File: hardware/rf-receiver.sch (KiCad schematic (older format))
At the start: 33 parts, among them IC1 ATSAMD21G18A-AU, J3 USB_C_Receptacle, P1 ROT_ENC, SW1 BTN1, SW2 BTN2, SW3 BTN3, U1 74HC14, Y1 Crystal_Small

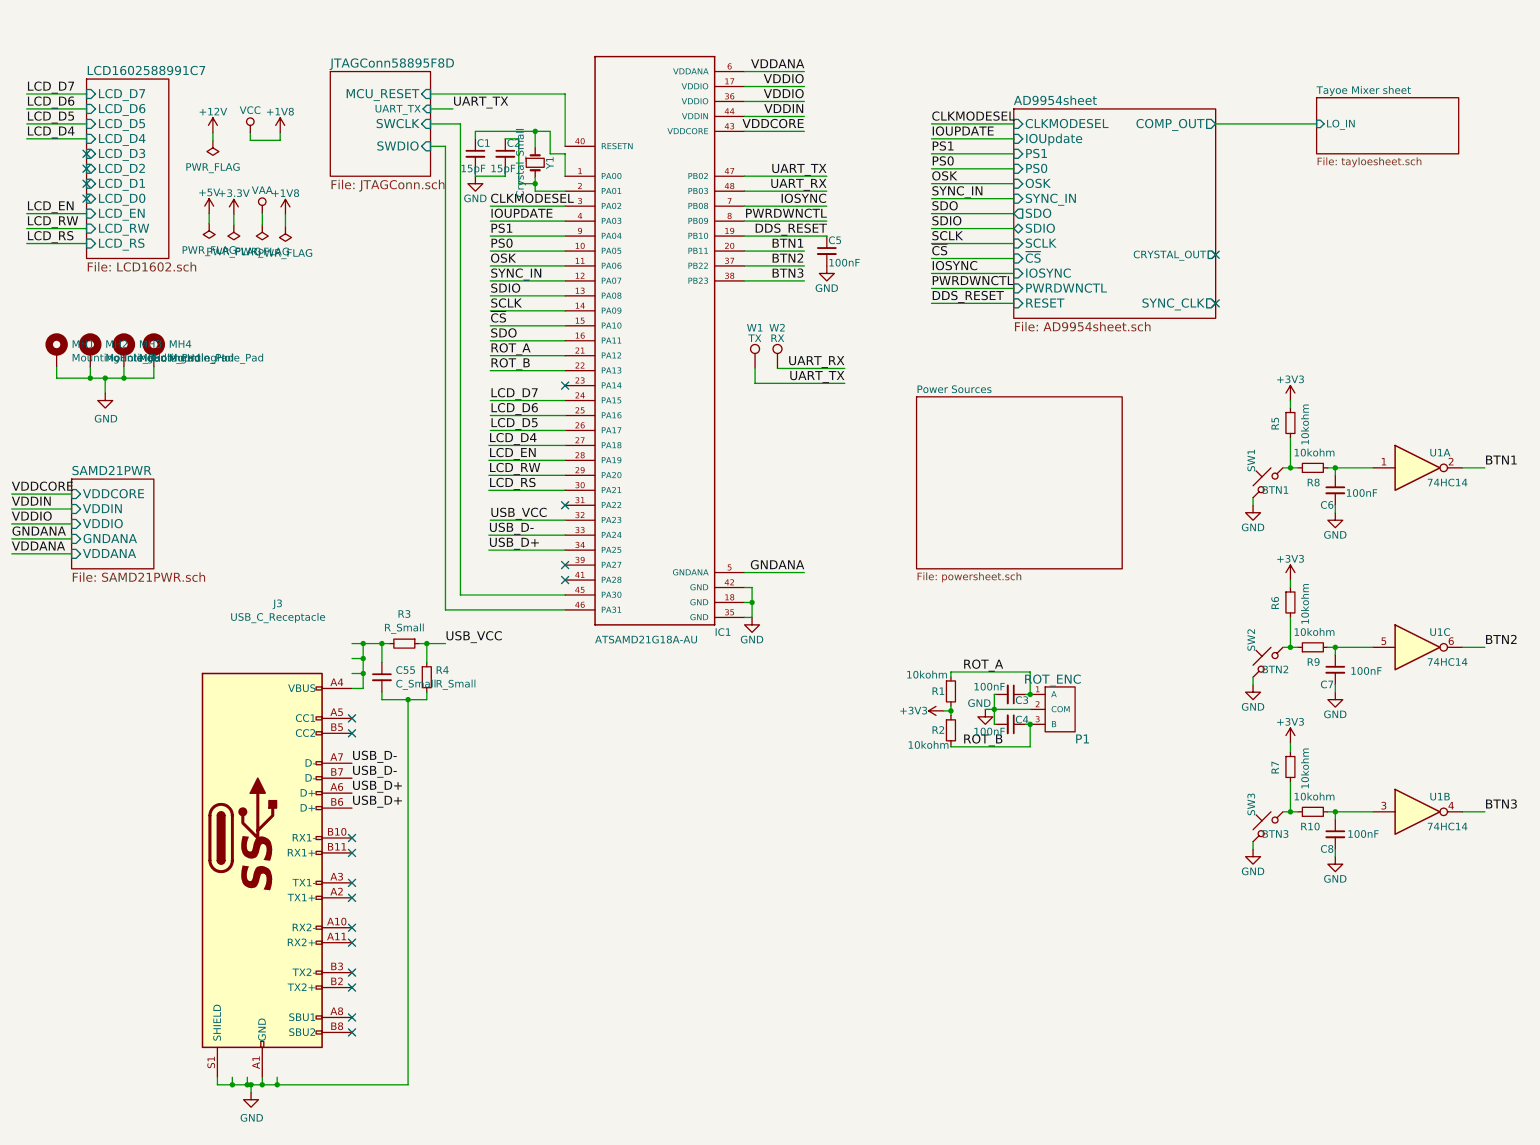
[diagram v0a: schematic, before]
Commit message: Finished work on Receiver RPi shield. Changed CLK to SI5351A. Minimized footprints for almost all Tayloe detector ICs. Added -12V to audio opamps. Prepared board for coexisting with Hifiberry.
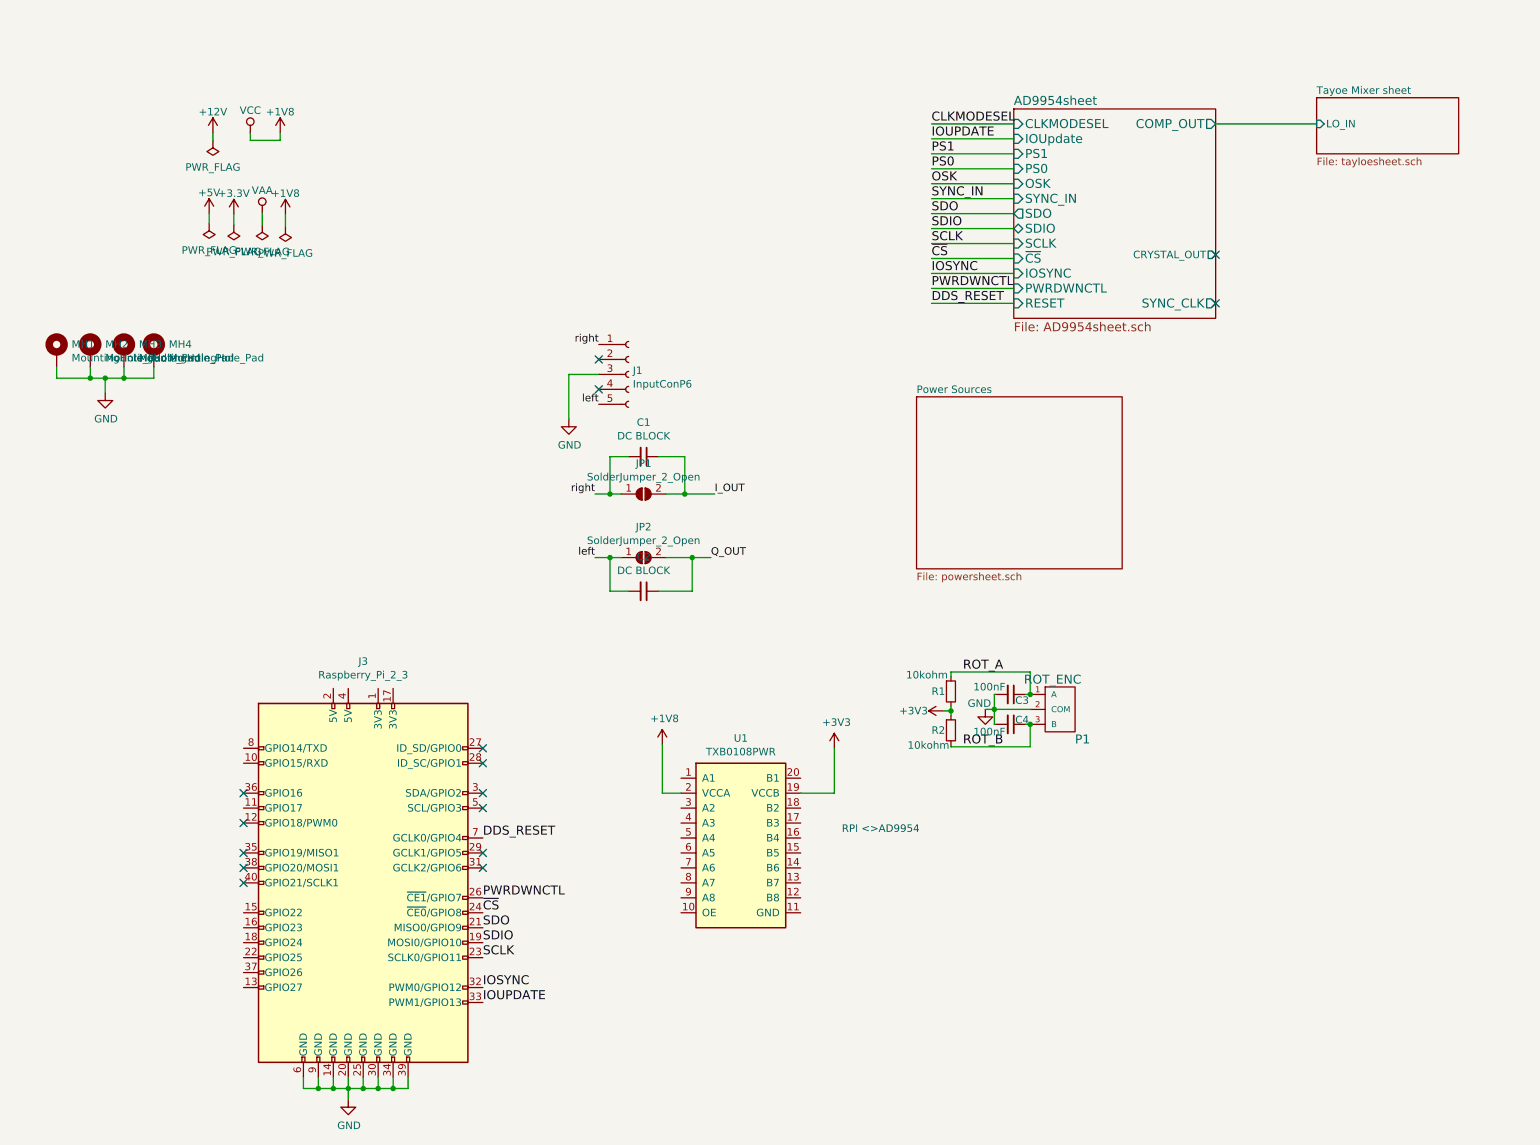
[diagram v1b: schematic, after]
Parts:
- removed C5, C6, C7, C8: 100nF, Capacitor_SMD:C_0603_1608Metric, symbol Device:C_Small
- removed C55: C_Small, Capacitor_SMD:C_0603_1608Metric, symbol Device:C_Small
- removed IC1: ATSAMD21G18A-AU, Package_QFP:TQFP-48_7x7mm_P0.5mm, symbol athir:ATSAMD21G18A-AU
- removed J3: USB_C_Receptacle, athir:DX07S024JJ, symbol Connector:USB_C_Receptacle
- removed R10, R5, R6, R7, R8, R9: 10kohm, Resistor_SMD:R_0603_1608Metric, symbol Device:R_Small
- removed R3, R4: R_Small, Resistor_SMD:R_0603_1608Metric, symbol Device:R_Small
- removed SW1: BTN1, Connector_PinHeader_2.54mm:PinHeader_1x02_P2.54mm_Vertical, symbol Switch:SW_Push_45deg
- removed SW2: BTN2, Connector_PinHeader_2.54mm:PinHeader_1x02_P2.54mm_Vertical, symbol Switch:SW_Push_45deg
- removed SW3: BTN3, Connector_PinHeader_2.54mm:PinHeader_1x02_P2.54mm_Vertical, symbol Switch:SW_Push_45deg
- removed U1: 74HC14, Package_SO:TSSOP-14_4.4x5mm_P0.65mm, symbol 74xx:74HC14
- removed W1: TX, TestPoint:TestPoint_THTPad_2.0x2.0mm_Drill1.0mm, symbol Connector:TestPoint
- removed W2: RX, TestPoint:TestPoint_THTPad_2.0x2.0mm_Drill1.0mm, symbol Connector:TestPoint
- removed Y1: Crystal_Small, Crystal:Crystal_SMD_3215-2Pin_3.2x1.5mm, symbol Device:Crystal_Small
- added J1: InputConP6, Connector_PinHeader_2.54mm:PinHeader_1x05_P2.54mm_Vertical, symbol Connector:Conn_01x05_Female
- added J3: Raspberry_Pi_2_3, Connector_PinHeader_2.54mm:PinHeader_2x20_P2.54mm_Vertical, symbol Connector:Raspberry_Pi_2_3
- added JP1, JP2: SolderJumper_2_Open, symbol Jumper:SolderJumper_2_Open
- added U1: TXB0108PWR, TO_SOT_Packages_SMD:USON-20_2x4mm_Pitch0.4mm, symbol athir:TXB0108PWR
- C1, C2: value 15pF -> DC BLOCK
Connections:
- net labels added: I_OUT, Q_OUT, left, right
- net labels removed: BTN1, BTN2, BTN3, GNDANA, LCD_D4, LCD_D5, LCD_D6, LCD_D7, LCD_EN, LCD_RS, LCD_RW, UART_RX, UART_TX, USB_D+, USB_D-, USB_VCC, VDDANA, VDDCORE, VDDIN, VDDIO
- wire segments 189 -> 86
- no-connect marks 22 -> 15
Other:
- note added: "RPI <>AD9954"

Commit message: Added rpi changes - seems weird that I forgot that for so long
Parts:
- removed JP1, JP2: SolderJumper_2_Open, symbol Jumper:SolderJumper_2_Open
- removed U1: TXB0108PWR, TO_SOT_Packages_SMD:USON-20_2x4mm_Pitch0.4mm, symbol athir:TXB0108PWR
- added C14, C15: 39pF, Capacitor_SMD:C_0603_1608Metric, symbol Device:C_Small
- added C16, C17, C20, C23: 100nF, Capacitor_SMD:C_0603_1608Metric, symbol Device:C_Small
- added C18, C19: 10uF, Capacitor_SMD:C_0603_1608Metric, symbol Device:C_Small
- added C7: 22uF, Capacitor_SMD:C_0805_2012Metric, symbol Device:C_Small
- added D1, D2: LED, Diode_SMD:D_1206_3216Metric, symbol Device:LED
- added J8: RF_Shield_One_Piece, RF_Shielding:Laird_Technologies_BMI-S-101_13.66x12.70mm, symbol Device:RF_Shield_One_Piece
- added JP1: Jumper_2_Open, Connector_PinHeader_2.54mm:PinHeader_1x02_P2.54mm_Vertical, symbol Jumper:Jumper_2_Open
- added R3, R9: 100, Resistor_SMD:R_0805_2012Metric, symbol Device:R_Small
- added R4: 1k, Resistor_SMD:R_0603_1608Metric, symbol Device:R_Small
- added R5, R8: 3k9, Resistor_SMD:R_0603_1608Metric, symbol Device:R_Small
- added R6, R7: I2CPULLUP, Resistor_SMD:R_0603_1608Metric, symbol Device:R_Small
- added TP13: SCL, athir:testpoint_probe, symbol Connector:TestPoint
- added TP2: SDA, athir:testpoint_probe, symbol Connector:TestPoint
- added U1: MIC5504-3.3YM5, Package_TO_SOT_SMD:SOT-23-5, symbol Regulator_Linear:MIC5504-3.3YM5
- added U2: CAT24C128, Package_SO:SOIC-8_3.9x4.9mm_P1.27mm, symbol Memory_EEPROM:CAT24C128
- added U3: SI5351A-B-GT, digikey-footprints:MSOP-10_W3mm, symbol dk_Clock-Timing-Clock-Generators-PLLs-Frequency-Synthesizers:SI5351A-B-GT
- added Y1: 25MHz 20pF, Crystal:Crystal_SMD_3225-4Pin_3.2x2.5mm, symbol Device:Crystal_GND24
- J1: footprint Connector_PinHeader_2.54mm:PinHeader_1x05_P2.54mm_Vertical -> Connector_PinSocket_2.54mm:PinSocket_1x05_P2.54mm_Vertical
- J3: footprint Connector_PinHeader_2.54mm:PinHeader_2x20_P2.54mm_Vertical -> Connector_PinSocket_2.54mm:PinSocket_2x20_P2.54mm_Vertical
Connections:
- net +3V3: now also C23.2, R4.1, R5.1, R8.1, U2.8 (VCC)
- net +5V: now also J3.2 (5V), J3.4 (5V), C18.1, C7.1, U1.1 (VIN), U1.3 (EN)
- net GND: now also C14.1, C15.1, C16.2, C17.1, C18.2, C19.2, C20.2, C23.1, C7.2, D1.1 (K), D2.1 (K), J8.1 (Shield), JP1.2 (B), U1.2 (GND), U2.1 (A0), U2.2 (A1), U2.3 (A2), U2.4 (GND), U3.8 (GND), Y1.2, Y1.4
- net ROT_A: now also J3.15 (GPIO22)
- net ROT_B: now also J3.16 (GPIO23)
- net SDA: now reaches J3.3 (SDA/GPIO2)
- net SDA: now also R7.2, R8.2, TP2.1, U2.5 (SDA), U3.5 (SDA)
- net SCL: now reaches J3.5 (SCL/GPIO3)
- net SCL: now also R5.2, R6.2, TP13.1, U2.6 (SCL), U3.4 (SCL)
- net DDS_RESET: no longer names the net of J3.7 (GCLK0/GPIO4)
- net IOSYNC: no longer names the net of J3.32 (PWM0/GPIO12)
- net IOSYNC: now also R3.1
- net IOUPDATE: no longer names the net of J3.33 (PWM1/GPIO13)
- net IOUPDATE: now also R9.1
- net PWRDWNCTL: no longer names the net of J3.26 (~CE1~/GPIO7)
- net SCLK: no longer names the net of J3.23 (SCLK0/GPIO11)
- net SDIO: no longer names the net of J3.19 (MOSI0/GPIO10)
- net SDO: no longer names the net of J3.21 (MISO0/GPIO9)
- net ~CS: no longer names the net of J3.24 (~CE0~/GPIO8)
- new net: C15.2, U3.2 (XA), Y1.1
- new net: C14.2, U3.3 (XB), Y1.3
- new net: D1.2 (A), R3.2
- new net: JP1.1 (A), R4.2, U2.7 (WP)
- new net: D2.2 (A), R9.2
- new net +3.3VA: C16.1, C17.2, C19.1, C20.1, R6.1, R7.1, U1.5 (VOUT), U3.1 (VDD), U3.7 (VDDO)
- new net Tayoe Mixer sheet/LO_IN: U3.10 (CLK0)
- no-connect marks 15 -> 28
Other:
- note removed: "RPI <>AD9954"

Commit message: HW: Fixed SMA footprint and 74x3253 footprint
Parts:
- added TP16, TP17: TestPoint, athir:testpoint_probe, symbol Connector:TestPoint
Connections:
- net GND: now also TP17.1
- net Tayoe Mixer sheet/LO_IN: now also TP16.1
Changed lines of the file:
@@
 Connection ~ 10075 5575
 Wire Wire Line
-	8900 1075 9250 1075
+	8900 1075 9150 1075
 Wire Wire Line
 	9250 1075 9250 1100
@@
 Wire Wire Line
 	4835 6710 4835 6830
+$Comp
+L Connector:TestPoint TP16
+U 1 1 5E57B516
+P 9150 975
+F 0 "TP16" H 9208 1093 50  0000 L CNN
+F 1 "TestPoint" H 9208 1002 50  0000 L CNN
+F 2 "athir:testpoint_probe" H 9350 975 50  0001 C CNN
+F 3 "~" H 9350 975 50  0001 C CNN
+	1    9150 975
+	1    0    0    -1
+$EndComp
+Wire Wire Line
+	9150 975  9150 1075
+Connection ~ 9150 1075
+Wire Wire Line
+	9150 1075 9250 1075
+$Comp
+L Connector:TestPoint TP17
+U 1 1 5E58AEC5
+P 9150 1375
+F 0 "TP17" H 9208 1493 50  0000 L CNN
+F 1 "TestPoint" H 9208 1402 50  0000 L CNN
+F 2 "athir:testpoint_probe" H 9350 1375 50  0001 C CNN
+F 3 "~" H 9350 1375 50  0001 C CNN
+	1    9150 1375
+	1    0    0    -1
+$EndComp
+$Comp
+L power:GND #PWR03
+U 1 1 5E58B9E2
+P 9150 1450
+F 0 "#PWR03" H 9150 1200 50  0001 C CNN
+F 1 "GND" H 9155 1277 50  0000 C CNN
+F 2 "" H 9150 1450 50  0001 C CNN
+F 3 "" H 9150 1450 50  0001 C CNN
+	1    9150 1450
+	1    0    0    -1
+$EndComp
+Wire Wire Line
+	9150 1450 9150 1375
 $EndSCHEMATC

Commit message: Sorry future me
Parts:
- added C31: 22uF, Capacitor_SMD:C_0805_2012Metric, symbol Device:C_Small
- added C32: 100nF, Capacitor_SMD:C_0603_1608Metric, symbol Device:C_Small
- added TP20, TP21: TestPoint, athir:testpoint_probe, symbol Connector:TestPoint
- MH1, MH2, MH3, MH4: footprint MountingHole:MountingHole_2.7mm_M2.5_Pad -> MountingHole:MountingHole_3.2mm_M3_Pad
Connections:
- net +5V: now also C31.1, C32.2
- net GND: now also C31.2, C32.1
- net at U3.6 (CLK2): now also TP21.1
- net at U3.9 (CLK1): now also TP20.1
- no-connect marks 28 -> 26
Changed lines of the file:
@@
 $Descr A4 11693 8268
 encoding utf-8
-Sheet 1 3
+Sheet 1 4
 Title ""
 Date "2019-01-20"
@@
 F 0 "MH1" H 1100 2676 50  0000 L CNN
 F 1 "MountingHole_Pad" H 1100 2585 50  0000 L CNN
-F 2 "MountingHole:MountingHole_2.7mm_M2.5_Pad" H 1000 2625 50  0001 C CNN
+F 2 "MountingHole:MountingHole_3.2mm_M3_Pad" H 1000 2625 50  0001 C CNN
 F 3 "~" H 1000 2625 50  0001 C CNN
 	1    1000 2625
@@
 F 0 "MH2" H 1325 2676 50  0000 L CNN
 F 1 "MountingHole_Pad" H 1325 2585 50  0000 L CNN
-F 2 "MountingHole:MountingHole_2.7mm_M2.5_Pad" H 1225 2625 50  0001 C CNN
+F 2 "MountingHole:MountingHole_3.2mm_M3_Pad" H 1225 2625 50  0001 C CNN
 F 3 "~" H 1225 2625 50  0001 C CNN
 	1    1225 2625
@@
 F 0 "MH3" H 1550 2676 50  0000 L CNN
 F 1 "MountingHole_Pad" H 1550 2585 50  0000 L CNN
-F 2 "MountingHole:MountingHole_2.7mm_M2.5_Pad" H 1450 2625 50  0001 C CNN
+F 2 "MountingHole:MountingHole_3.2mm_M3_Pad" H 1450 2625 50  0001 C CNN
 F 3 "~" H 1450 2625 50  0001 C CNN
 	1    1450 2625
@@
 F 0 "MH4" H 1750 2676 50  0000 L CNN
 F 1 "MountingHole_Pad" H 1750 2585 50  0000 L CNN
-F 2 "MountingHole:MountingHole_2.7mm_M2.5_Pad" H 1650 2625 50  0001 C CNN
+F 2 "MountingHole:MountingHole_3.2mm_M3_Pad" H 1650 2625 50  0001 C CNN
 F 3 "~" H 1650 2625 50  0001 C CNN
 	1    1650 2625
@@
 Wire Wire Line
 	9250 1100 9425 1100
-NoConn ~ 8900 1175
-NoConn ~ 8900 1275
 Text Label 3850 5575 0    50   ~ 0
 SDA
@@
 $EndComp
 Wire Wire Line
-	2575 4775 2575 4700
+	2575 4775 2575 4735
 $Comp
 L power:-12V #PWR?
@@
 Wire Wire Line
 	9150 1450 9150 1375
+$Comp
+L Device:C_Small C?
+U 1 1 5E716223
+P 2395 4605
+AR Path="/5C517D7D/5E716223" Ref="C?"  Part="1"
+AR Path="/5E716223" Ref="C31"  Part="1"
+F 0 "C31" H 2487 4651 50  0000 L CNN
+F 1 "22uF" H 2487 4560 50  0000 L CNN
+F 2 "Capacitor_SMD:C_0805_2012Metric" H 2395 4605 50  0001 C CNN
+F 3 "~" H 2395 4605 50  0001 C CNN
+	1    2395 4605
+	1    0    0    -1
+$EndComp
+Wire Wire Line
+	2575 4475 2395 4475
+Wire Wire Line
+	2395 4475 2395 4505
+Connection ~ 2575 4475
+Wire Wire Line
+	2395 4705 2395 4735
+Wire Wire Line
+	2395 4735 2575 4735
+Connection ~ 2575 4735
+Wire Wire Line
+	2575 4735 2575 4700
+$Comp
+L Device:C_Small C32
+U 1 1 5E733990
+P 2220 4605
+F 0 "C32" V 2190 4635 50  0000 L CNN
+F 1 "100nF" V 2270 4355 50  0000 L CNN
+F 2 "Capacitor_SMD:C_0603_1608Metric" H 2220 4605 50  0001 C CNN
+F 3 "" H 2220 4605 50  0000 C CNN
+	1    2220 4605
+	-1   0    0    1
+$EndComp
+Wire Wire Line
+	2395 4475 2220 4475
+Wire Wire Line
+	2220 4475 2220 4505
+Connection ~ 2395 4475
+Wire Wire Line
+	2220 4705 2220 4735
+Wire Wire Line
+	2220 4735 2395 4735
+Connection ~ 2395 4735
+$Comp
+L Connector:TestPoint TP20
+U 1 1 5E6E2812
+P 8955 1160
+F 0 "TP20" H 9013 1278 50  0000 L CNN
+F 1 "TestPoint" H 9013 1187 50  0000 L CNN
+F 2 "athir:testpoint_probe" H 9155 1160 50  0001 C CNN
+F 3 "~" H 9155 1160 50  0001 C CNN
+	1    8955 1160
+	1    0    0    -1
+$EndComp
+$Comp
+L Connector:TestPoint TP21
+U 1 1 5E6E4E81
+P 9000 1260
+F 0 "TP21" H 9058 1378 50  0000 L CNN
+F 1 "TestPoint" H 9058 1287 50  0000 L CNN
+F 2 "athir:testpoint_probe" H 9200 1260 50  0001 C CNN
+F 3 "~" H 9200 1260 50  0001 C CNN
+	1    9000 1260
+	1    0    0    -1
+$EndComp
+Wire Wire Line
+	8900 1275 9000 1275
+Wire Wire Line
+	9000 1275 9000 1260
+Wire Wire Line
+	8955 1175 8900 1175
+Wire Wire Line
+	8955 1175 8955 1160
 $EndSCHEMATC
